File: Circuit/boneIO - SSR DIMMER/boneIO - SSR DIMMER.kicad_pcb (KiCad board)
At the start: 2 copper layers, 197 x 102 mm, 209 parts, among them J1 Conn_02x04_Odd_Even, J10 Screw_Terminal_01x04, J11 Screw_Terminal_01x04, J12 Screw_Terminal_01x04, J13 Screw_Terminal_01x04, J2 DIMMER, J3 DIMMER, J4 DIMMER, J5 DIMMER, J6 DIMMER, J7 DIMMER, J8 Screw_Terminal_01x04, J9 Screw_Terminal_01x04, Q1 BT136-600, Q10 BT136-600, Q11 BT136-600, Q12 BT136-600, Q13 BTA12-600B, Q14 BTA12-600B, Q15 BTA12-600B, Q16 BTA12-600B, Q17 BTA12-600B, Q18 BTA12-600B, Q19 BTA12-600B, Q2 BT136-600, Q20 BTA12-600B, Q21 BTA12-600B, Q22 BTA12-600B, Q23 BTA12-600B, Q24 BTA12-600B, Q3 BT136-600, Q4 BT136-600, Q5 BT136-600, Q6 BT136-600, Q7 BT136-600, Q8 BT136-600, Q9 BT136-600, U1 MCP9808-E_SO8, U10 MOC3041M, U11 MOC3041M, U12 MOC3041M, U13 MOC3041M, U14 MOC3041M, U15 MOC3041M, U16 MOC3041M, U17 MOC3041M, U18 MOC3041M, U19 MOC3041M, U2 MCP9808-E_MS, U20 MOC3041M, U21 MOC3041M, U22 MOC3041M, U23 MOC3041M, U24 MOC3041M, U25 MOC3041M, U26 MOC3041M, U27 MOC3041M, U28 MOC3041M, U29 MOC3041M, U3 PCA9685PW, U30 MOC3041M, U31 MOC3041M, U4 MOC3041M, U5 ULN2803A, U6 ULN2803A, U7 MOC3041M, U8 MCP23017_SS

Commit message: Add files via upload
Poprawione
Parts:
- removed R1, R14, R15, R2, R3: 0k_NC, Resistor_SMD:R_0603_1608Metric
- removed R12, R16, R33, R34, R35, R8, R9: 0k, Resistor_SMD:R_0603_1608Metric
- added G***: LOGO, Symbol:boneIO_LOGO_srednie, F.Cu at (66.9, 88.7)
- added JP10: Jumper_NO_Small, Jumper:SolderJumper-2_P1.3mm_Open_RoundedPad1.0x1.5mm, F.Cu at (172.6, 92.0)
- added JP11: Jumper_NO_Small, Jumper:SolderJumper-2_P1.3mm_Open_RoundedPad1.0x1.5mm, F.Cu at (175.2, 92.0)
- added JP12: Jumper_NO_Small, Jumper:SolderJumper-2_P1.3mm_Open_RoundedPad1.0x1.5mm, F.Cu at (177.7, 92.0)
- added JP2: Jumper_NO_Small, Jumper:SolderJumper-2_P1.3mm_Open_RoundedPad1.0x1.5mm, F.Cu at (228.5, 87.3)
- added JP3: Jumper_NO_Small, Jumper:SolderJumper-2_P1.3mm_Open_RoundedPad1.0x1.5mm, F.Cu at (228.5, 90.0)
- added JP4: Jumper_NO_Small, Jumper:SolderJumper-2_P1.3mm_Open_RoundedPad1.0x1.5mm, F.Cu at (125.6, 90.6)
- added JP5: Jumper_NO_Small, Jumper:SolderJumper-2_P1.3mm_Open_RoundedPad1.0x1.5mm, F.Cu at (128.9, 90.6)
- added JP6: Jumper_NO_Small, Jumper:SolderJumper-2_P1.3mm_Open_RoundedPad1.0x1.5mm, F.Cu at (132.2, 90.6)
- added JP7: Jumper_NO_Small, Jumper:SolderJumper-2_P1.3mm_Open_RoundedPad1.0x1.5mm, F.Cu at (164.8, 92.0)
- added JP8: Jumper_NO_Small, Jumper:SolderJumper-2_P1.3mm_Open_RoundedPad1.0x1.5mm, F.Cu at (167.4, 92.0)
- added JP9: Jumper_NO_Small, Jumper:SolderJumper-2_P1.3mm_Open_RoundedPad1.0x1.5mm, F.Cu at (170.0, 92.0)
- JP1: value SolderJumper_3_Bridged12 -> Jumper_NO_Small; footprint Jumper:SolderJumper-3_P1.3mm_Bridged12_RoundedPad1.0x1.5mm -> Jumper:SolderJumper-2_P1.3mm_Open_RoundedPad1.0x1.5mm
- R17, R18, R36, R37, R38, R39, R4, R40, R41, R5, R6: value 0k -> 10k
- R19: value 0k_NC -> 10k
- U2: footprint Package_SO:SO-8_3.9x4.9mm_P1.27mm -> Package_SO:MSOP-8_3x3mm_P0.65mm
- moved JP1 89.1 mm to (228.5, 84.7)
- moved C1 87.6 mm to (230.9, 95.0), turned to 270 degrees
- moved R32 76.7 mm to (229.9, 92.3), turned to 0 degrees
- moved U1 67.9 mm to (221.5, 92.1)
- moved R7 67.6 mm to (229.1, 95.0), turned to 270 degrees
- moved U2 59.3 mm to (221.5, 92.1), turned to 270 degrees
- moved R6 49.9 mm to (219.3, 86.8), turned to 180 degrees
- moved R4 49.8 mm to (219.2, 83.5), turned to 180 degrees
- moved R5 49.8 mm to (219.2, 85.1), turned to 180 degrees
- moved U6 27.8 mm to (203.6, 88.8)
- moved C3 23.4 mm to (101.1, 84.9), turned to 270 degrees
- moved C4 18.6 mm to (202.2, 95.6), turned to 180 degrees
- moved R13 17.5 mm to (124.7, 93.2), turned to 180 degrees
- moved U5 15.8 mm to (92.8, 88.8), turned to 90 degrees
- moved R36 12.8 mm to (164.8, 88.4)
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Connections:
- C3 pad 1: VCC -> +5V
- C4 pad 1: VCC -> +5V
- JP1 pad 1: +5V -> +3V3
- JP1 pad 2: VCC -> Net-(JP1-Pad2)
- R4 pad 1: Net-(R1-Pad2) -> Net-(JP1-Pad2)
- U1 pad 7: Net-(R1-Pad2) -> Net-(JP1-Pad2)
- U2 pad 7: Net-(R1-Pad2) -> Net-(JP1-Pad2)
- U5 pad 10: VCC -> +5V
- U6 pad 10: VCC -> +5V
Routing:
- net GND: track 592.0 -> 9.91 mm, vias 82 -> 114
- net VCC: track 175.5 -> 0.00 mm, vias 3 -> 0
- net +5V: track 3.57 -> 168.4 mm, vias 0 -> 3
- net Net-(R1-Pad2): track 48.6 -> 0.00 mm, vias 2 -> 0
- net +3V3: track 166.8 -> 205.0 mm, vias 4 -> 2
- net SDA: track 107.2 -> 143.5 mm
- net K2: track 54.9 -> 25.4 mm
- net K7: track 56.3 -> 29.4 mm, vias 2 -> 0
- net RELAY7: track 104.7 -> 79.2 mm, vias 2 -> 0
- net K10: track 130.0 -> 105.3 mm
- net K12: track 132.7 -> 110.0 mm
- net Net-(JP1-Pad2): track 0.00 -> 21.8 mm, vias 0 -> 2
- net SCL: track 120.4 -> 140.6 mm, vias 2 -> 5
- net RELAY8: track 79.9 -> 59.9 mm, vias 1 -> 0
- net RELAY10: track 60.5 -> 40.6 mm, vias 0 -> 3
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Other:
- board text added: "12x SSR & 12x Dimmer Board v0.3"

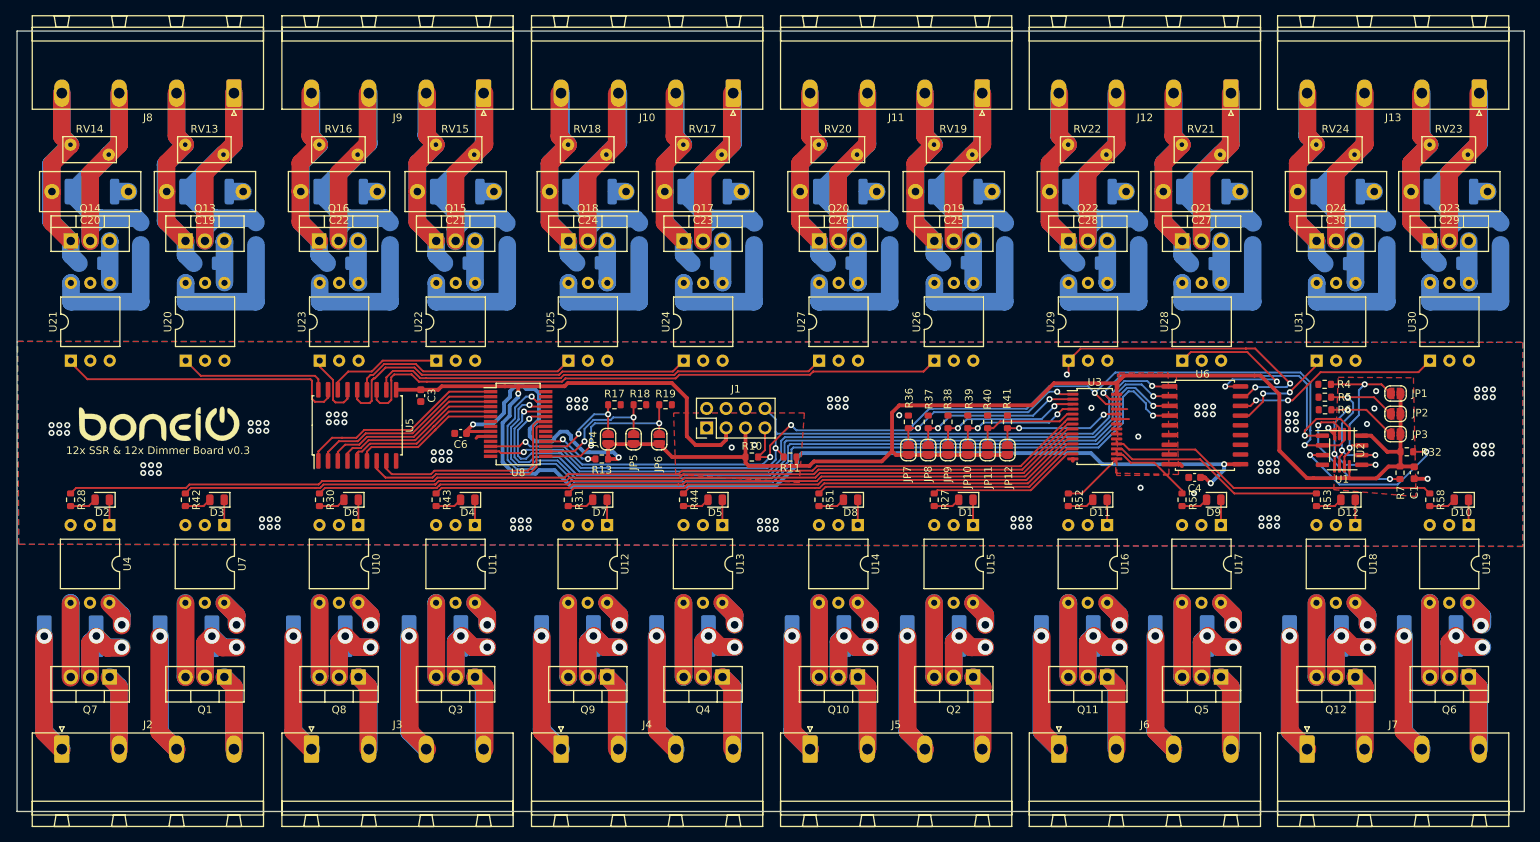
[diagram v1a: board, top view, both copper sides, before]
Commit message: Add files via upload
Poprawione według wskazówek. Wszystkie elementy z jednej strony. Wzmocnione ścieżki HV. Poprawiona numeracja płyty.
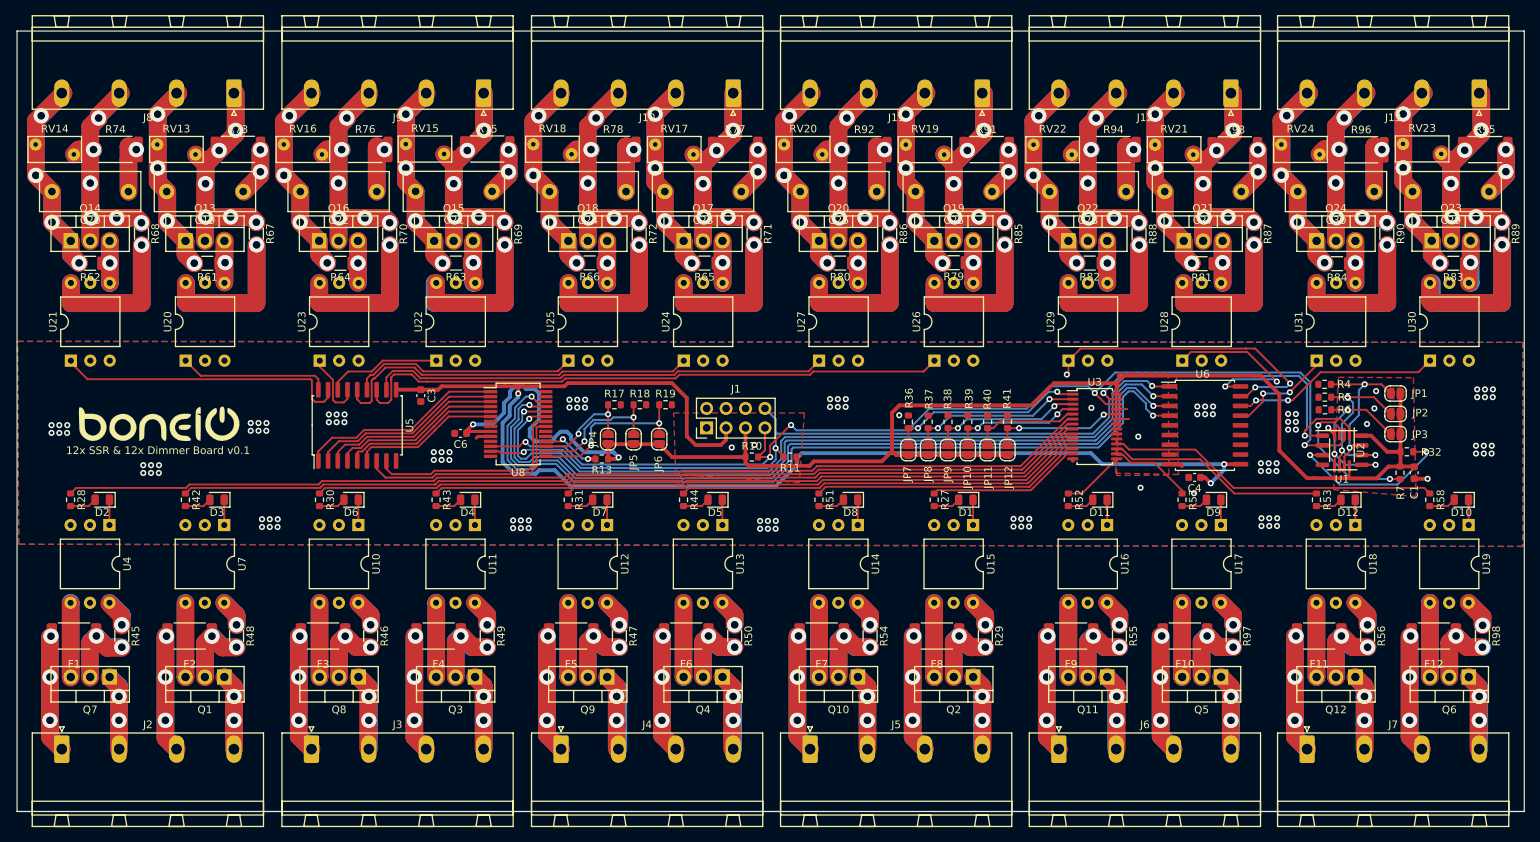
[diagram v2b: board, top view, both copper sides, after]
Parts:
- F1, F10, F11, F12, F2, F3, F4, F5, F6, F7, F8, F9: footprint Fuse:Fuse_2920_7451Metric -> Fuse:Fuse_2512_6332Metric; moved to F.Cu
- R29, R45, R46, R47, R48, R49, R50, R54, R55, R56, R61, R62, R63, R64, R65, R66, R67, R68, R69, R70, R71, R72, R73, R74, R75, R76, R77, R78, R79, R80, R81, R82, R83, R84, R85, R86, R87, R88, R89, R90, R91, R92, R93, R94, R95, R96, R97, R98: moved to F.Cu
- moved R95 7.08 mm to (240.2, 52.8)
- moved R73 6.86 mm to (77.2, 52.8)
- moved R91 6.84 mm to (175.0, 52.8)
- moved R93 6.84 mm to (207.5, 52.8)
- moved R77 6.80 mm to (142.2, 52.8)
- moved R75 6.80 mm to (109.8, 52.7)
- moved R76 6.37 mm to (93.8, 52.8)
- moved R78 6.32 mm to (126.2, 52.8)
- moved R92 6.31 mm to (159.0, 52.8)
- moved R94 6.31 mm to (191.6, 52.8)
- moved R74 6.31 mm to (61.2, 52.8)
- moved R96 6.27 mm to (224.0, 52.8)
- moved RV16 4.64 mm to (88.2, 53.4)
- moved RV24 4.57 mm to (218.5, 53.4)
- moved RV14 4.56 mm to (55.7, 53.4)
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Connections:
- R29 pad 1: Net-(F8-Pad1) -> Net-(R29-Pad2)
- R29 pad 2: Net-(R29-Pad2) -> Net-(F8-Pad1)
- R45 pad 1: Net-(F1-Pad1) -> Net-(R45-Pad2)
- R45 pad 2: Net-(R45-Pad2) -> Net-(F1-Pad1)
- R46 pad 1: Net-(F3-Pad1) -> Net-(R46-Pad2)
- R46 pad 2: Net-(R46-Pad2) -> Net-(F3-Pad1)
- R47 pad 1: Net-(F5-Pad1) -> Net-(R47-Pad2)
- R47 pad 2: Net-(R47-Pad2) -> Net-(F5-Pad1)
- R48 pad 1: Net-(F2-Pad1) -> Net-(R48-Pad2)
- R48 pad 2: Net-(R48-Pad2) -> Net-(F2-Pad1)
- R49 pad 1: Net-(F4-Pad1) -> Net-(R49-Pad2)
- R49 pad 2: Net-(R49-Pad2) -> Net-(F4-Pad1)
- R50 pad 1: Net-(F6-Pad1) -> Net-(R50-Pad2)
- R50 pad 2: Net-(R50-Pad2) -> Net-(F6-Pad1)
- R54 pad 1: Net-(F7-Pad1) -> Net-(R54-Pad2)
- R54 pad 2: Net-(R54-Pad2) -> Net-(F7-Pad1)
- R55 pad 1: Net-(F9-Pad1) -> Net-(R55-Pad2)
- R55 pad 2: Net-(R55-Pad2) -> Net-(F9-Pad1)
- R56 pad 1: Net-(F11-Pad1) -> Net-(R56-Pad2)
- R56 pad 2: Net-(R56-Pad2) -> Net-(F11-Pad1)
- R97 pad 1: Net-(F10-Pad1) -> Net-(R97-Pad2)
- R97 pad 2: Net-(R97-Pad2) -> Net-(F10-Pad1)
- R98 pad 1: Net-(F12-Pad1) -> Net-(R98-Pad2)
- R98 pad 2: Net-(R98-Pad2) -> Net-(F12-Pad1)
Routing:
- net Net-(R68-Pad2): track 19.0 -> 39.0 mm, vias 0 -> 1
- net Net-(R88-Pad2): track 19.0 -> 39.0 mm, vias 0 -> 1
- net Net-(R90-Pad2): track 19.1 -> 39.0 mm, vias 0 -> 1
- net Net-(R70-Pad2): track 19.1 -> 39.0 mm, vias 0 -> 1
- net Net-(R86-Pad2): track 19.1 -> 39.0 mm, vias 0 -> 1
- net Net-(R89-Pad2): track 19.1 -> 38.9 mm, vias 0 -> 1
- net Net-(R72-Pad2): track 19.1 -> 39.0 mm, vias 0 -> 1
- net Net-(R67-Pad2): track 19.1 -> 38.9 mm, vias 0 -> 1
- net Net-(R85-Pad2): track 19.1 -> 38.9 mm, vias 0 -> 1
- net Net-(R71-Pad2): track 19.1 -> 38.9 mm, vias 0 -> 1
- net Net-(R87-Pad2): track 19.1 -> 38.9 mm, vias 0 -> 1
- net Net-(R69-Pad2): track 19.2 -> 38.7 mm, vias 0 -> 1
- net Net-(C22-Pad1): track 1.19 -> 14.4 mm, vias 0 -> 1
- net Net-(C20-Pad1): track 1.19 -> 14.4 mm, vias 0 -> 1
- net Net-(C30-Pad1): track 1.19 -> 14.4 mm, vias 0 -> 1
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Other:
- board text added: "12x SSR & 12x Dimmer Board v0.1"
- board text removed: "12x SSR & 12x Dimmer Board v0.3"

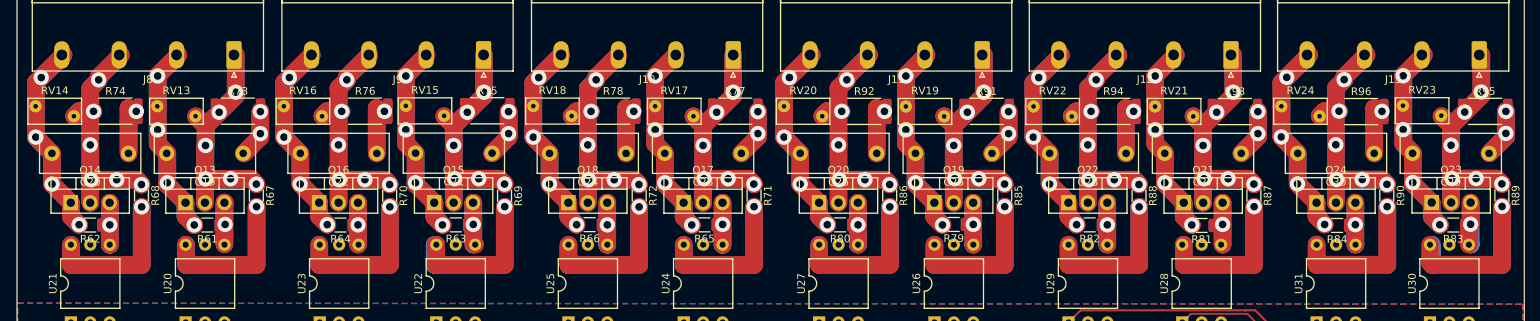
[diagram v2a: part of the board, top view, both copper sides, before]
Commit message: Add files via upload
Przesunięte triaki i warystory.
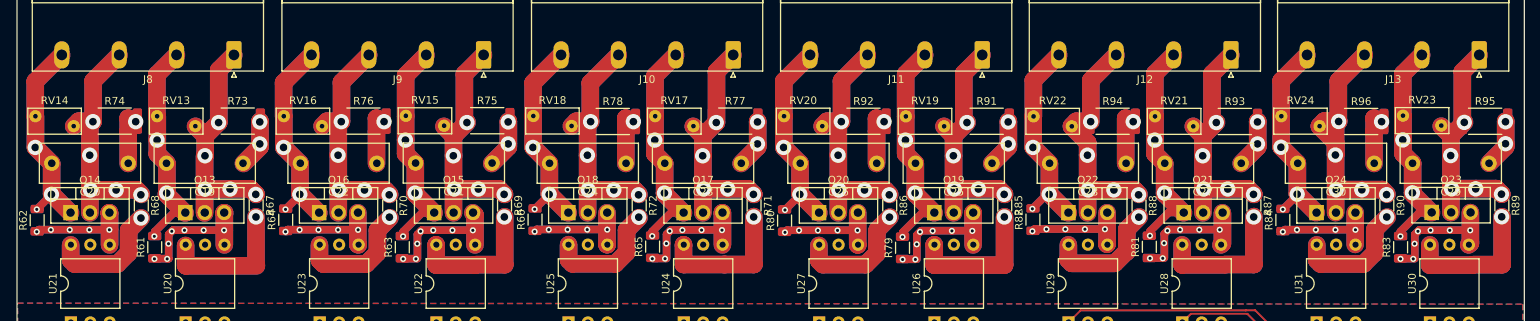
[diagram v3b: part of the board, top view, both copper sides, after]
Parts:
- moved R63 7.59 mm to (98.7, 70.5), turned to 90 degrees
- moved R61 7.47 mm to (66.3, 70.5), turned to 90 degrees
- moved R83 7.47 mm to (229.1, 70.5), turned to 90 degrees
- moved R82 7.45 mm to (181.1, 66.9), turned to 90 degrees
- moved R81 7.38 mm to (196.3, 70.5), turned to 90 degrees
- moved R79 7.36 mm to (164.0, 70.6), turned to 90 degrees
- moved R65 7.35 mm to (131.4, 70.5), turned to 90 degrees
- moved R80 7.29 mm to (148.6, 67.1), turned to 90 degrees
- moved R64 7.20 mm to (83.4, 67.0), turned to 90 degrees
- moved R66 7.17 mm to (116.0, 66.9), turned to 90 degrees
- moved R84 7.12 mm to (213.7, 67.0), turned to 90 degrees
- moved R62 6.96 mm to (50.9, 67.0), turned to 90 degrees
- moved R78 1.35 mm to (126.2, 54.1)
- moved R76 1.32 mm to (93.6, 54.1)
- moved R92 1.30 mm to (158.9, 54.1)
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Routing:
- net Net-(Q13-Pad3): track 11.0 -> 33.5 mm, vias 1 -> 7
- net Net-(Q21-Pad3): track 11.0 -> 33.2 mm, vias 1 -> 7
- net Net-(Q15-Pad3): track 11.1 -> 33.3 mm, vias 1 -> 7
- net Net-(Q23-Pad3): track 11.1 -> 33.3 mm, vias 1 -> 7
- net Net-(Q17-Pad3): track 11.0 -> 33.1 mm, vias 1 -> 7
- net Net-(Q19-Pad3): track 11.0 -> 33.1 mm, vias 1 -> 7
- net Net-(Q14-Pad3): track 11.0 -> 27.6 mm, vias 1 -> 5
- net Net-(Q16-Pad3): track 11.0 -> 27.6 mm, vias 1 -> 5
- net Net-(Q20-Pad3): track 11.0 -> 27.6 mm, vias 1 -> 5
- net Net-(Q18-Pad3): track 11.0 -> 27.5 mm, vias 1 -> 5
- net Net-(Q24-Pad3): track 11.0 -> 27.4 mm, vias 1 -> 5
- net Net-(Q22-Pad3): track 11.0 -> 27.4 mm, vias 1 -> 5
- net Net-(J13-Pad3): track 61.2 -> 72.8 mm, vias 6 -> 5
- net Net-(R88-Pad2): track 39.0 -> 31.1 mm
- net Net-(R86-Pad2): track 39.0 -> 31.3 mm
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
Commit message: Add files via upload
Jumpery po stronie bottom.
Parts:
- JP1, JP10, JP11, JP12, JP2, JP3, JP4, JP5, JP6, JP7, JP8, JP9: moved to B.Cu
- turned JP4 to 270 degrees
- turned JP5 to 270 degrees
- turned JP6 to 270 degrees
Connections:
- JP4 pad 1: +3V3 -> Net-(JP4-Pad2)
- JP4 pad 2: Net-(JP4-Pad2) -> +3V3
- JP5 pad 1: +3V3 -> Net-(JP5-Pad2)
- JP5 pad 2: Net-(JP5-Pad2) -> +3V3
- JP6 pad 1: +3V3 -> Net-(JP6-Pad2)
- JP6 pad 2: Net-(JP6-Pad2) -> +3V3
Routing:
- net SCL: track 140.6 -> 150.9 mm
- net SDA: track 143.5 -> 147.9 mm
- net +5V: track 168.4 -> 166.7 mm
- net K12: track 110.0 -> 111.0 mm
- net K11: track 107.5 -> 108.3 mm
- net K10: track 105.3 -> 105.9 mm
- net K9: track 102.9 -> 103.5 mm
- net Net-(JP7-Pad2): vias 2 -> 3
- net +3V3: vias 2 -> 14
- net Net-(JP8-Pad2): vias 2 -> 3
- net Net-(JP9-Pad2): vias 2 -> 3
- net Net-(JP6-Pad2): vias 2 -> 3
- net Net-(JP5-Pad2): vias 2 -> 3
- net Net-(JP4-Pad2): vias 2 -> 3
- net Net-(JP3-Pad2): vias 3 -> 4
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
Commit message: Poprawiana wersja
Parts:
- renumbered JP7 to A0, JP6 to A0, JP1 to A0, JP8 to A1, JP5 to A1, JP2 to A1, JP9 to A2, JP4 to A2, JP3 to A2, JP10 to A3, JP11 to A4, JP12 to A5
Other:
- board text added: "DOWN"
- board text added: "WARNING!!!"
